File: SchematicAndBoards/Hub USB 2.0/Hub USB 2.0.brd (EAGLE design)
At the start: 61.9 x 17.8 mm, 29 parts, among them IC1 STM32F10XCXT6, IC2 MCP1703CB, IC3 IC_USBLC6-2, Q1 KX-7T 16.0 MHz, X1 USB-A

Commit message: Update schematic and boards
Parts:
- IC1: device stm32F:TQFP48 -> stm32:TQFP48
- IC3: value IC_USBLC6-2 -> USBLC6
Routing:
- net VDD3.3: track 99.5 -> 100.1 mm
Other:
- board size 61.9 x 17.8 mm -> 63.2 x 17.8 mm
- board text added: "RST"
- board text added: "RX TX"
- board text added: "SWCLK"
- board text added: "SWDIO"
- board text added: "SaeWave.com"
- board text removed: "SaeWave"

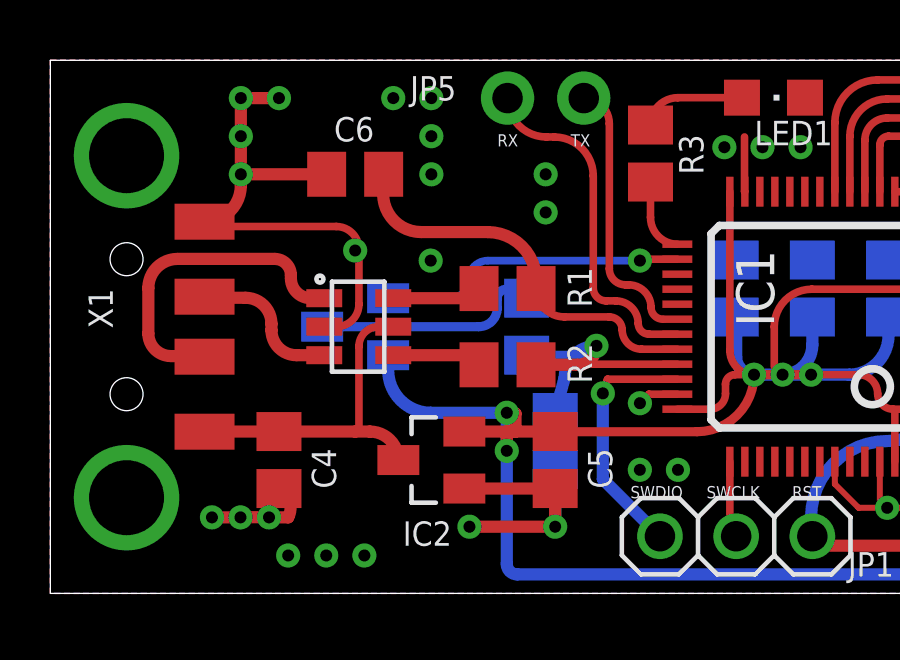
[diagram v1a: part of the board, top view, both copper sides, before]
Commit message: Update Hub USB 2.0 schematic
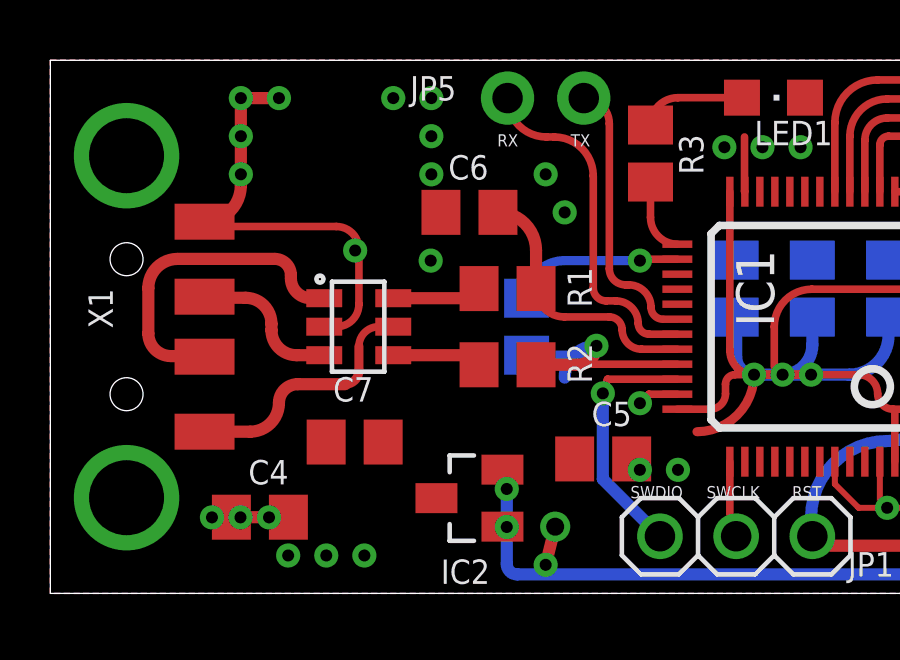
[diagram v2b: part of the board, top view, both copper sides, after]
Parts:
- removed Q2: (no value), semicon-smd-ipc:SOT23
- moved C7 6.68 mm to (10.1, 5.04), flipped to the top, turned to 0 degrees
- moved C6 4.02 mm to (14.0, 12.7)
- moved C4 2.01 mm to (6.99, 2.54), turned to 180 degrees
- moved IC2 1.80 mm to (14.0, 3.17)
- moved C5 1.60 mm to (18.4, 4.48), turned to 180 degrees
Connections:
- removed net N$8: Q2.3, R4.1
- net USB_DISC: now also R4.1; no longer Q2.1
- net VDD3.3: no longer Q2.2
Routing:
- net VDD3.3: track 100.1 -> 82.6 mm
- net GND: track 49.8 -> 38.2 mm, vias 42 -> 43
- net N$8: track 7.64 -> 0.00 mm
- net USB_DISC: track 10.2 -> 5.56 mm
- net N$10: track 12.8 -> 8.61 mm
- net VDD5: track 11.2 -> 8.21 mm
- net N$6: track 12.1 -> 10.9 mm

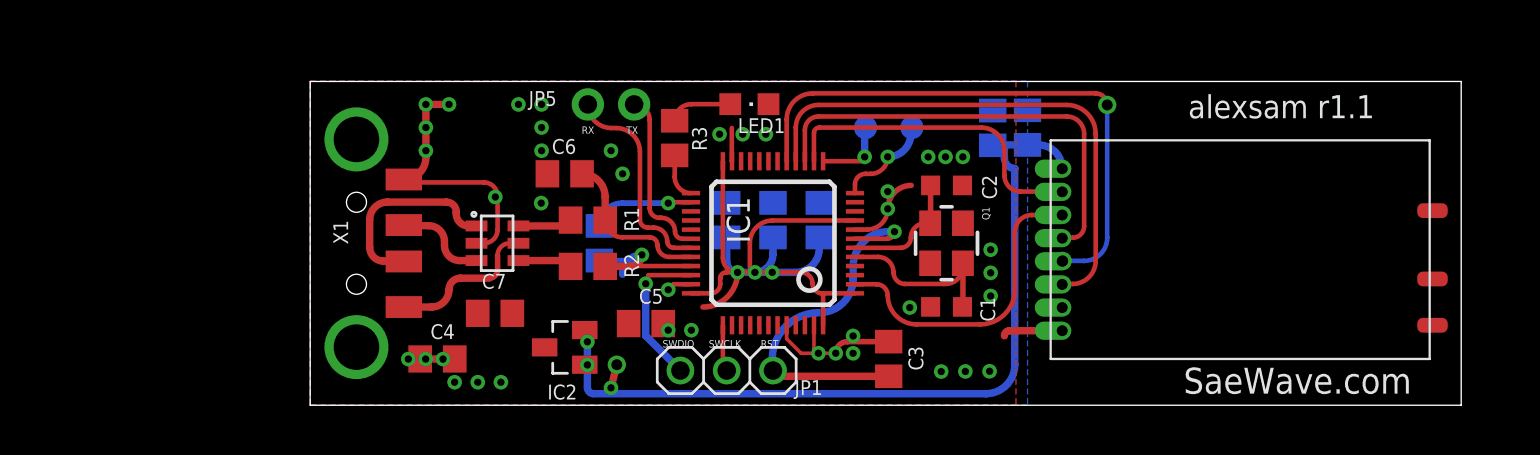
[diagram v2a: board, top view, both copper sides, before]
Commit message: Update Hub USB 2.0, add achematic in PDF
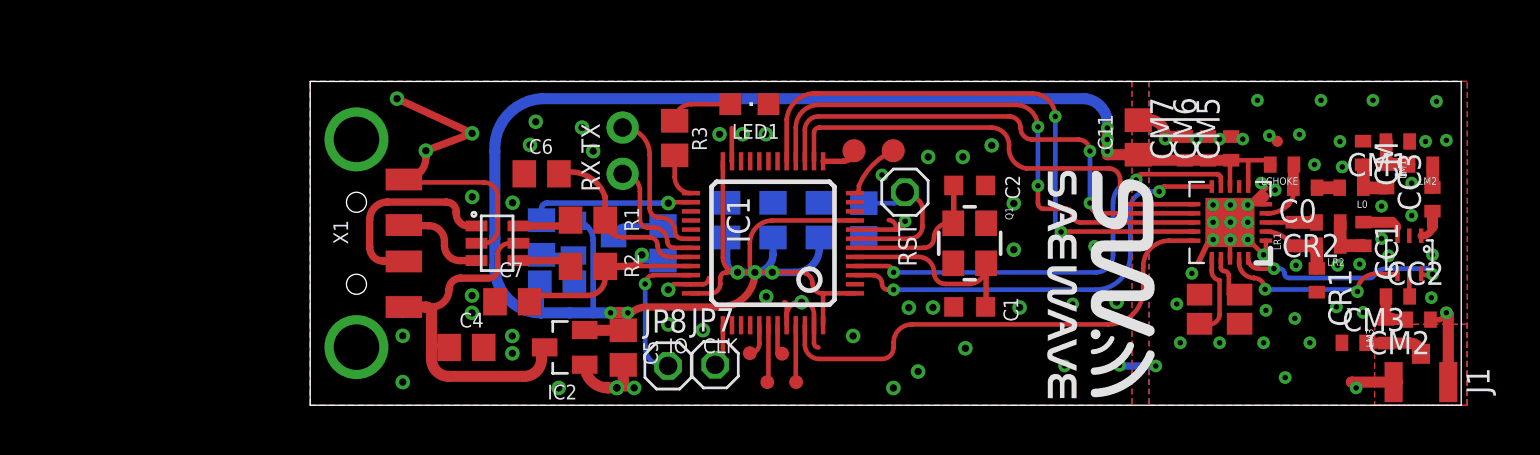
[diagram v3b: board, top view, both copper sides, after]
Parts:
- removed C12: 0.01uF, resistor:C0805
- added C0: 3.9pF, resistor:C0402
- added CC1, CC2, CC3: 56pF, resistor:C0402
- added CM: 5.6pF, resistor:C0402
- added CM1: 2.7pF, resistor:C0402
- added CM2, CM3: 4.3pF, resistor:C0402
- added CM5: 100pF, resistor:C0402
- added CM6: 100nF, resistor:C0402
- added CM7: 1u, resistor:C0402
- added CR1: 3pF, resistor:C0402
- added CR2: 1pF, resistor:C0402
- added J1: CON-HIROSE-COAXIAL-U.FL, m-pad-2.1:CON-U.FL
- added JP10, JP11, JP9: TEST-POINT3, SparkFun-Passives:PAD.03X.03
- added JP2, JP7, JP8: (no value), pinhead:1X01
- added L0: 12nH, SparkFun-Passives:C0402
- added LCHOKE: 100nH, SparkFun-Passives:C0402
- added LM1, LM2: 10nH, SparkFun-Passives:C0402
- added LM3: 8.2nH, SparkFun-Passives:C0402
- added LR1: 18nH, SparkFun-Passives:C0402
- added LR2: 22nH, SparkFun-Passives:C0402
- added Q2: (no value), adafruit:NX3225
- added Q3: FDN360P, transistor-power:SUPER-SOT3
- added R5: 10, resistor:R0805
- added R6: 10k, resistor:R0805
- added U$1: SI4464, Ava:QFN20+GNDPAD
- JP1: value (none) -> TEST-POINT3; device adafruit:1X03 -> SparkFun-Passives:PAD.03X.03
- LED1: value (none) -> LED
- Q1: value KX-7T 16.0 MHz -> 16.0 MHz
- U$2: value AS07-M1101S -> UPG2179TB; device RemoteSwitchComponents:AS07-M1101S -> Ava:SUPER_MINIMOLD
- moved U$2 9.55 mm to (60.3, 8.25), turned to 270 degrees
- moved C3 7.72 mm to (30.4, 10.1), flipped to the bottom, turned to 270 degrees
- moved C11 6.10 mm to (45.4, 14.7), flipped to the top
- moved JP6 4.26 mm to (17.1, 12.7)
- moved R4 3.49 mm to (19.4, 8.89)
- moved C5 1.81 mm to (17.2, 3.16), turned to 90 degrees
- moved C4 1.71 mm to (8.57, 3.17)
- moved JP3 1.63 mm to (32.0, 14.0), flipped to the top
- moved JP1 1.59 mm to (24.1, 2.86)
- moved JP5 1.42 mm to (17.1, 15.2)
- moved JP4 1.42 mm to (29.8, 14.0), flipped to the top
- moved C1 1.27 mm to (36.2, 5.40)
- moved C2 1.27 mm to (36.2, 12.1)
- moved Q1 1.27 mm to (36.2, 8.89)
- moved C6 1.27 mm to (12.7, 12.7)
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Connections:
- removed net VDD3.3: C10.2, C11.2, C12.2, C5.2, C8.2, C9.2, IC1.1, IC1.24, IC1.36, IC1.48, IC1.9, IC2.2, U$2.1
- new net ANT: CM3.2, J1.S, LM3.1
- new net GPIO0: IC1.4, U$1.9
- new net GPIO1: IC1.3, U$1.10
- new net N$11: CC3.1, U$2.1
- new net N$12: CR2.2, LR1.2, U$1.3
- new net N$13: CC1.1, U$2.3
- new net N$14: CR1.1, LR1.1, LR2.2, U$1.2
- new net N$16: CC2.2, U$2.5
- new net N$17: CC3.2, LM2.1
- new net N$18: CC1.2, CR2.1, LR2.1
- new net N$19: Q3.3, R4.1
- new net N$20: Q3.1, R5.1, R6.2
- new net N$3: C0.2, LCHOKE.1, U$1.4
- new net N$5: C0.1, L0.2
- new net N$7: CM.2, L0.1, LM1.2
- new net N$8: CM1.2, LM1.1, LM2.2
- new net N$9: CC2.1, CM2.2, LM3.2
- new net RF_GPIO2: U$1.19, U$2.4
- new net RF_GPIO3: U$1.20, U$2.6
- new net TEST-1: IC1.45, JP11.P$1
- new net TEST-2: IC1.43, JP10.P$1
- new net TEST-3: IC1.42, JP9.P$1
- new net TEST-4: IC1.41, JP1.P$1
- new net VDD: C10.2, C11.2, C5.2, C8.2, C9.2, CM5.1, CM6.1, CM7.1, IC1.1, IC1.24, IC1.36, IC1.48, IC1.9, IC2.2, LCHOKE.2, Q3.2, R6.1, U$1.6, U$1.8
- new net XTAIL-IN: Q2.1, U$1.17
- new net XTAIL-OUT: Q2.3, U$1.16
- net GND: now also CM.1, CM1.1, CM2.1, CM3.1, CM5.2, CM6.2, CM7.2, CR1.2, J1.GND@0, Q2.2, Q2.4, U$1.1, U$1.18, U$1.21, U$1.5, U$2.2; no longer C12.1, U$2.8
- net NIRQ: now also U$1.11; no longer U$2.2
- net NRST: now also JP2.1; no longer JP1.3
- net NSEL: now also IC1.46, U$1.15; no longer IC1.2, U$2.3
- net SPI1_MISO: now also U$1.13; no longer U$2.6
- net SPI1_MOSI: now also U$1.14; no longer U$2.5
- net SPI1_SCK: now also U$1.12; no longer U$2.4
- net SWCLK: now also JP7.1; no longer JP1.2
- net SWDIO: now also JP8.1; no longer JP1.1
- net USB_DISC: now also R5.2; no longer R4.1
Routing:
- net VDD: track 0.00 -> 122.6 mm, vias 0 -> 8
- net VDD3.3: track 82.6 -> 0.00 mm, vias 5 -> 0
- net GPIO0: track 0.00 -> 24.4 mm, vias 0 -> 2
- net GPIO1: track 0.00 -> 23.7 mm, vias 0 -> 2
- net GND: track 38.2 -> 59.4 mm, vias 43 -> 97
- net VDD5: track 8.21 -> 21.6 mm
- net RF_GPIO3: track 0.00 -> 11.5 mm, vias 0 -> 2
- net NRST: track 19.5 -> 8.79 mm, vias 1 -> 0
- net RF_GPIO2: track 0.00 -> 10.0 mm, vias 0 -> 2
- net NSEL: track 16.6 -> 26.3 mm
- net NIRQ: track 17.6 -> 25.0 mm
- net USART1_RX: track 11.1 -> 6.36 mm
- net XTAIL-OUT: track 0.00 -> 4.55 mm
- net N$14: track 0.00 -> 4.26 mm
- net N$3: track 0.00 -> 3.58 mm
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- added copper zone on layer 16, net N$22
- added copper zone on layer 1, net N$23
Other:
- board text added: "ANT"
- board text added: "CLK"
- board text added: "E:/Projects/STM32/RemoteSwitch/FWUpdater/SW_Logo-mono.bmp"
- board text added: "G0"
- board text added: "G1"
- board text added: "GND"
- board text added: "IO"
- board text added: "NIRQ"
- board text added: "NSEL"
- board text added: "SCLK"
- board text added: "SDI"
- board text added: "SDO"
- board text added: "VDD"
- board text removed: "SWCLK"
- board text removed: "SWDIO"
- board text removed: "SaeWave.com"
- board text removed: "alexsam r1.1"
